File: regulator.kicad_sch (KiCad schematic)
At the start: 13 parts, among them U1 LMR51450FNDRRR

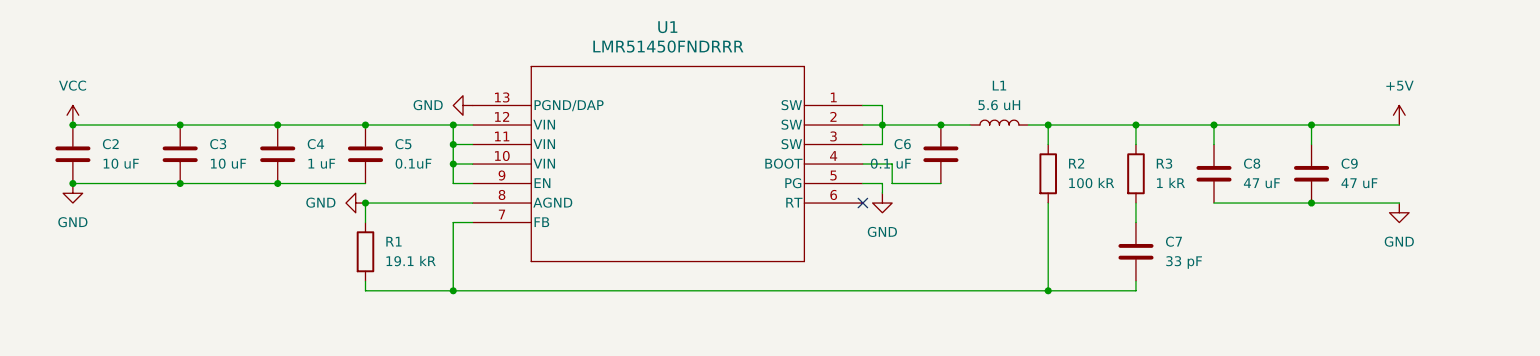
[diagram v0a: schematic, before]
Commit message: Endstops buffered & regulator 1MHz
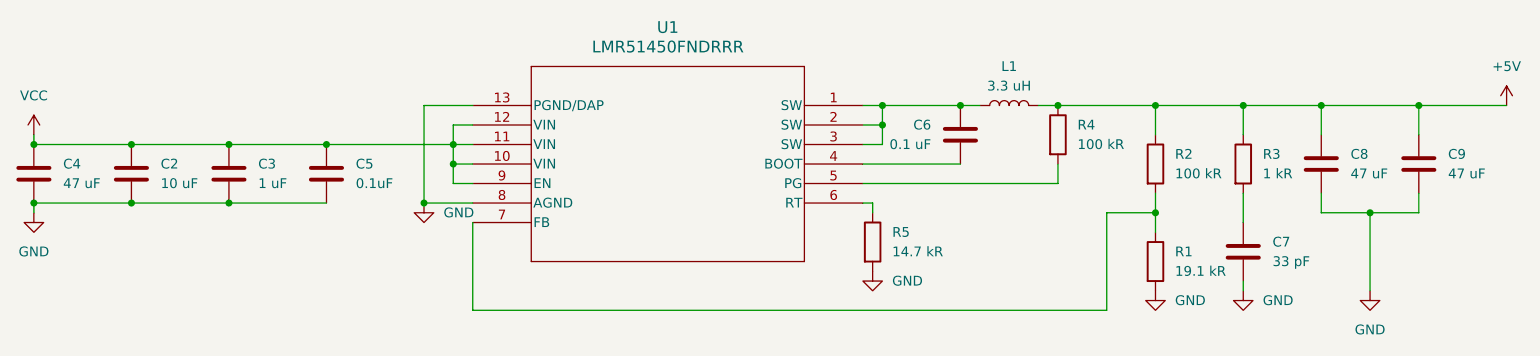
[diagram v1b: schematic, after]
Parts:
- added R4: 100 kR, Resistor_SMD:R_0603_1608Metric, symbol Device:R
- added R5: 14.7 kR, Resistor_SMD:R_0603_1608Metric, symbol Device:R
- C3: value 10 uF -> 1 uF
- C4: value 1 uF -> 47 uF; footprint Capacitor_SMD:C_0603_1608Metric -> Capacitor_SMD:C_1206_3216Metric
- L1: value 5.6 uH -> 3.3 uH
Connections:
- net +5V: now also R4.1
- net GND: now also C7.2, R1.2, R5.2; no longer R1.1, U1.5 (PG)
- net at U1.6 (RT): now also R5.1
- net at R2.2, U1.7 (FB): now also R1.1; no longer C7.2, R1.2
- new net: R4.2, U1.5 (PG)
- no-connect marks 1 -> 0
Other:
- moved on the sheet: C2, C3, C5, C6, C7, C8, C9, L1, R1, R2, R3
